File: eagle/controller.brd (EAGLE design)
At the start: 100 x 80 mm, 9 parts, among them IC1 ULN2003AD, IC2 ULN2003AD, U1 ARDUINO_PRO_MINI, X1 FH12-18S-0.5SH

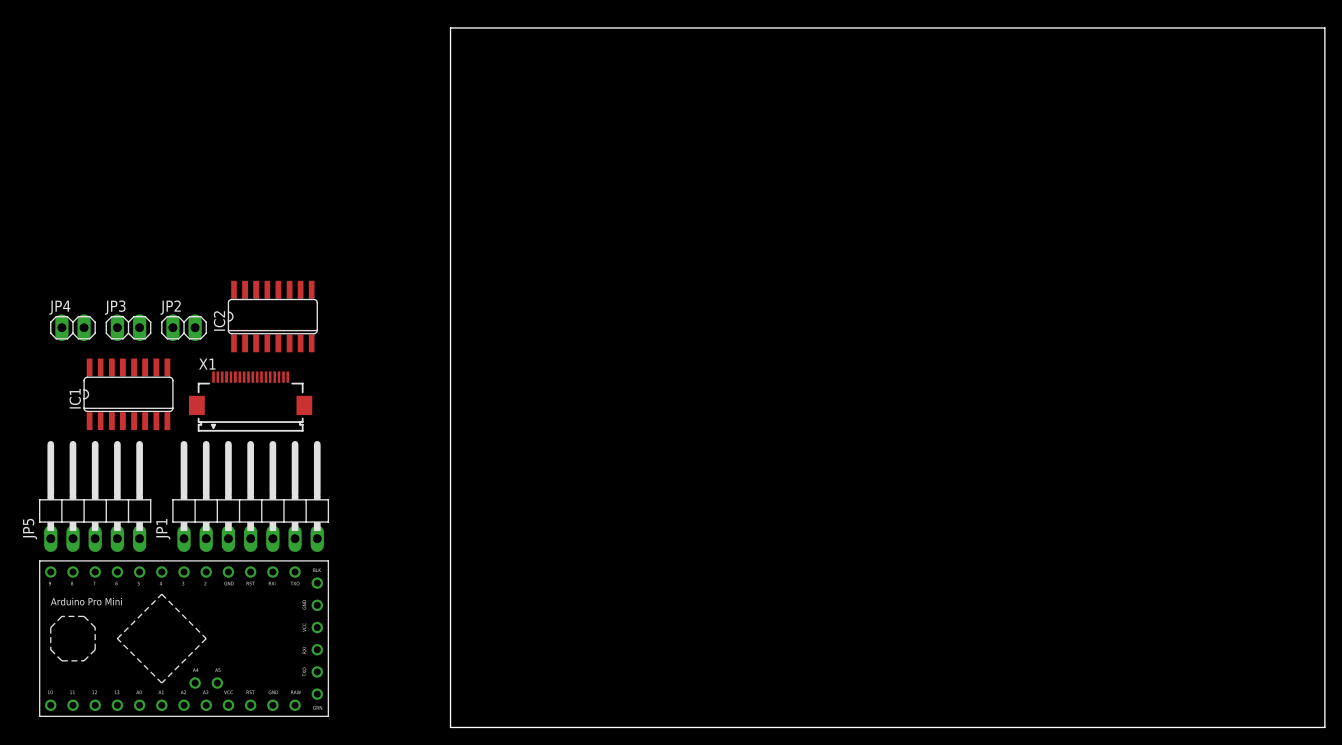
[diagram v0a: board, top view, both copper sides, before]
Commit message: routed the board, updated bom
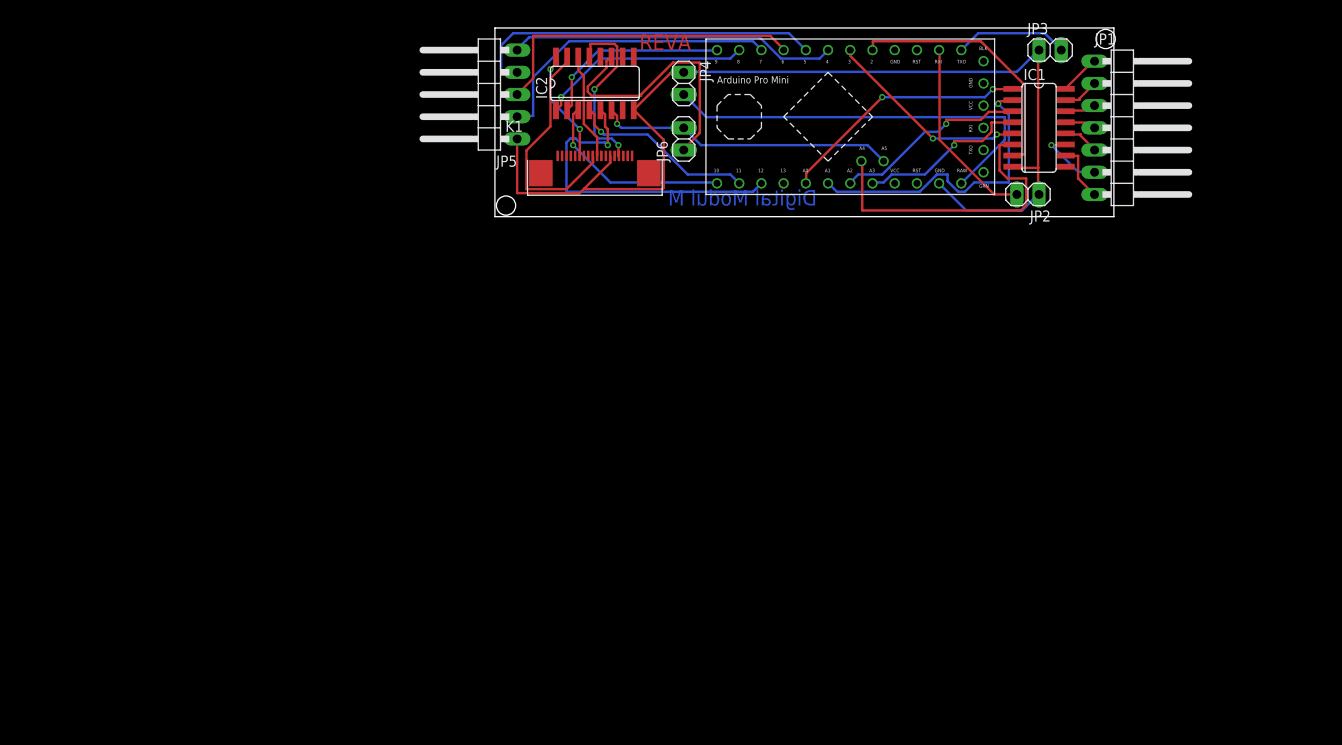
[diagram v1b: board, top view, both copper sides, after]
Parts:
- removed X1: FH12-18S-0.5SH, con-hirose:FH12-18S-0.5SH
- added JP6: Reserve, pinhead:1X02
- added K1: 68711814022, Wuerth_Elektronik_eiCan_03_ZIF_Connectors_Flat_Flexible_Cable:68711814022
- JP1: value (none) -> Emulation
- JP2: value (none) -> Release
- JP3: value (none) -> FAP
- JP4: value (none) -> Power
- JP5: value (none) -> ISO select
- moved JP3 110.1 mm to (68.6, 77.5)
- moved JP1 109.2 mm to (77.5, 68.6), turned to 270 degrees
- moved IC1 108.5 mm to (67.3, 68.6), turned to 270 degrees
- moved JP2 97.7 mm to (66.0, 61.0), turned to 180 degrees
- moved U1 96.8 mm to (47.0, 69.8)
- moved JP4 75.2 mm to (26.7, 73.7), turned to 270 degrees
- moved JP5 64.7 mm to (3.81, 72.4), turned to 90 degrees
- moved IC2 45.5 mm to (16.5, 73.7)
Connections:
- new net N$27: IC2.11, JP6.1
- new net N$28: IC2.16, K1.6
- new net N$29: IC2.15, K1.9
- new net N$30: IC2.14, K1.10
- new net N$31: IC2.13, K1.15
- net GND: now also K1.13
- net N$19: now also JP6.2
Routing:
- net GND: track 0.00 -> 121.0 mm
- net V+: track 0.00 -> 47.4 mm
- net N$14: track 0.00 -> 41.1 mm
- net N$12: track 0.00 -> 37.9 mm, vias 0 -> 1
- net N$13: track 0.00 -> 37.6 mm
- net N$15: track 0.00 -> 36.8 mm
- net N$6: track 0.00 -> 35.6 mm
- net N$2: track 0.00 -> 35.1 mm, vias 0 -> 1
- net N$16: track 0.00 -> 34.6 mm
- net N$19: track 0.00 -> 34.1 mm, vias 0 -> 1
- net N$27: track 0.00 -> 30.6 mm
- net N$7: track 0.00 -> 29.9 mm
- net N$1: track 0.00 -> 28.7 mm, vias 0 -> 2
- net N$29: track 0.00 -> 26.7 mm
- net N$8: track 0.00 -> 24.3 mm, vias 0 -> 1
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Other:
- board size 100 x 80 mm -> 70.8 x 21.6 mm
- board text added: "Digital Modul M"
- board text added: "REVA"
